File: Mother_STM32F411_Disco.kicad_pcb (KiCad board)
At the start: 2 copper layers, 234 x 132.7 mm, 34 parts, among them U1 ESP32-DEVKIT-V1

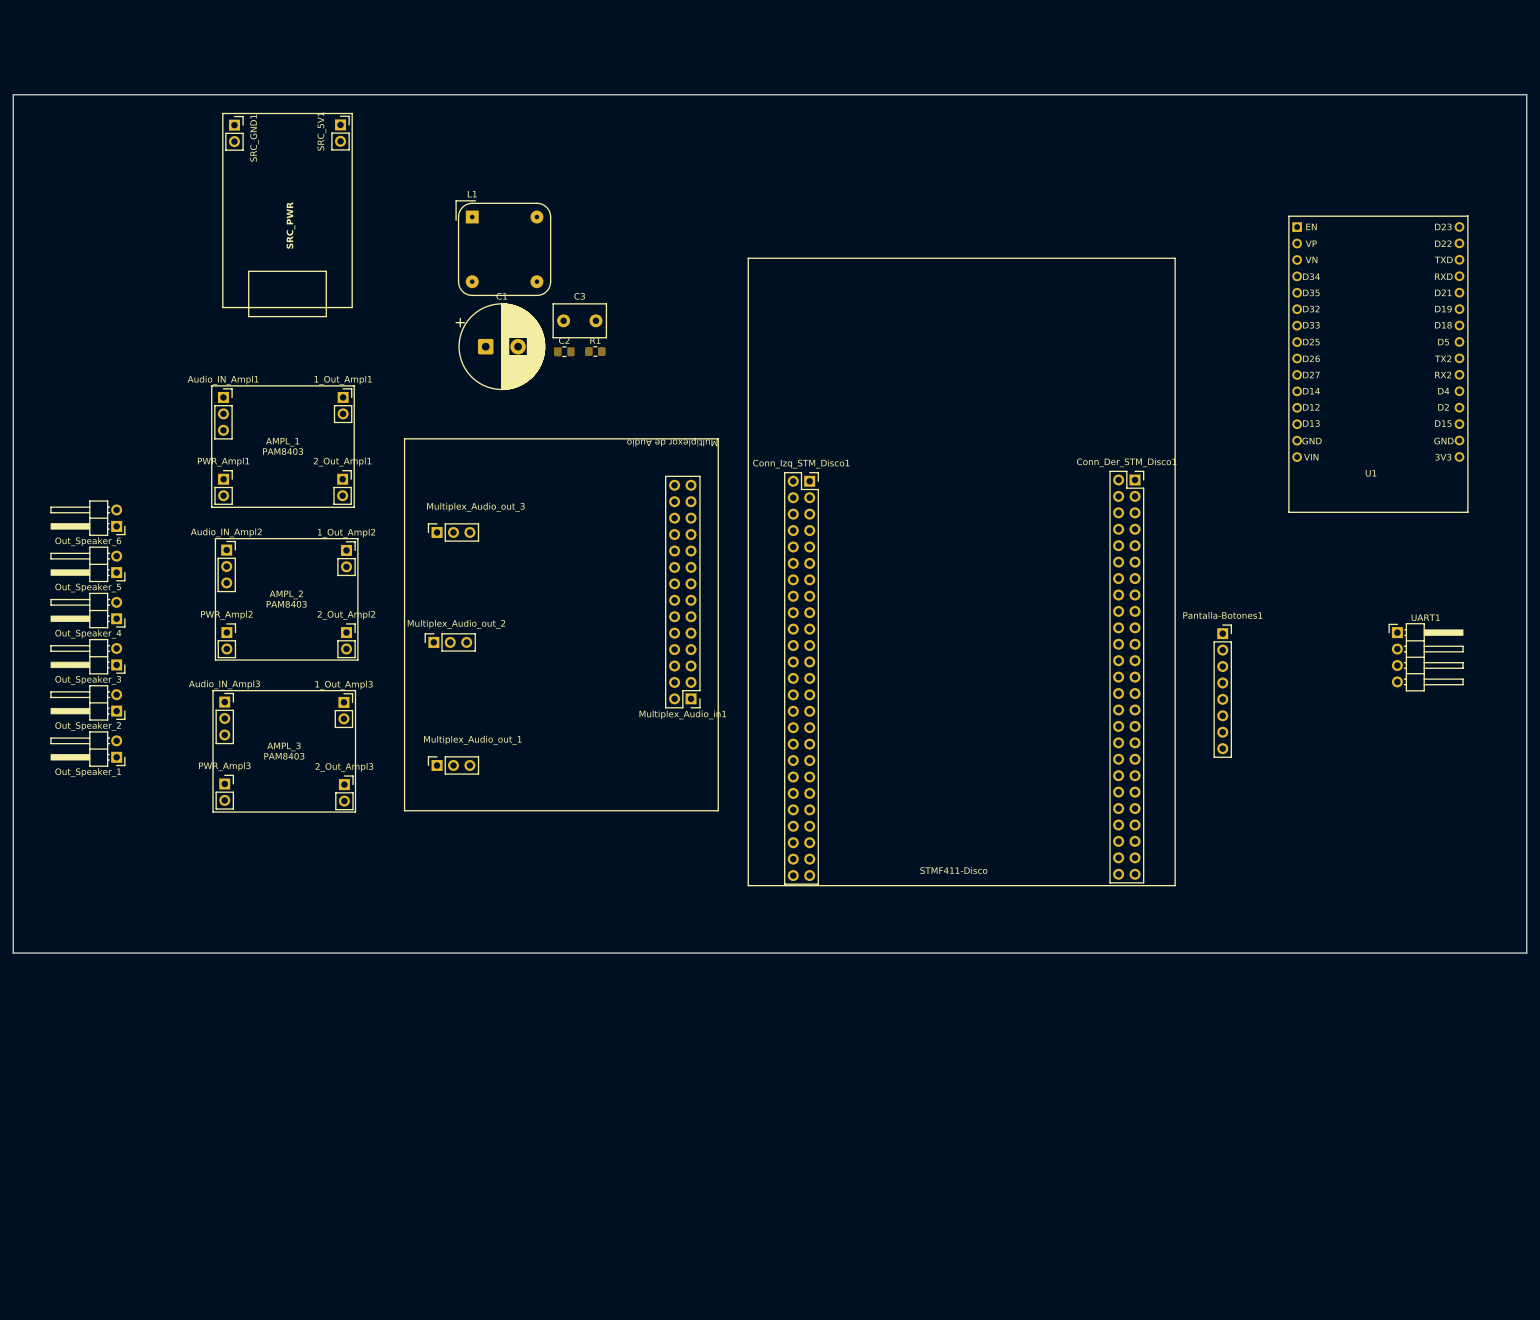
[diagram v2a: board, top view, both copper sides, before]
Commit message: Placa lista para ser routeada con pistas
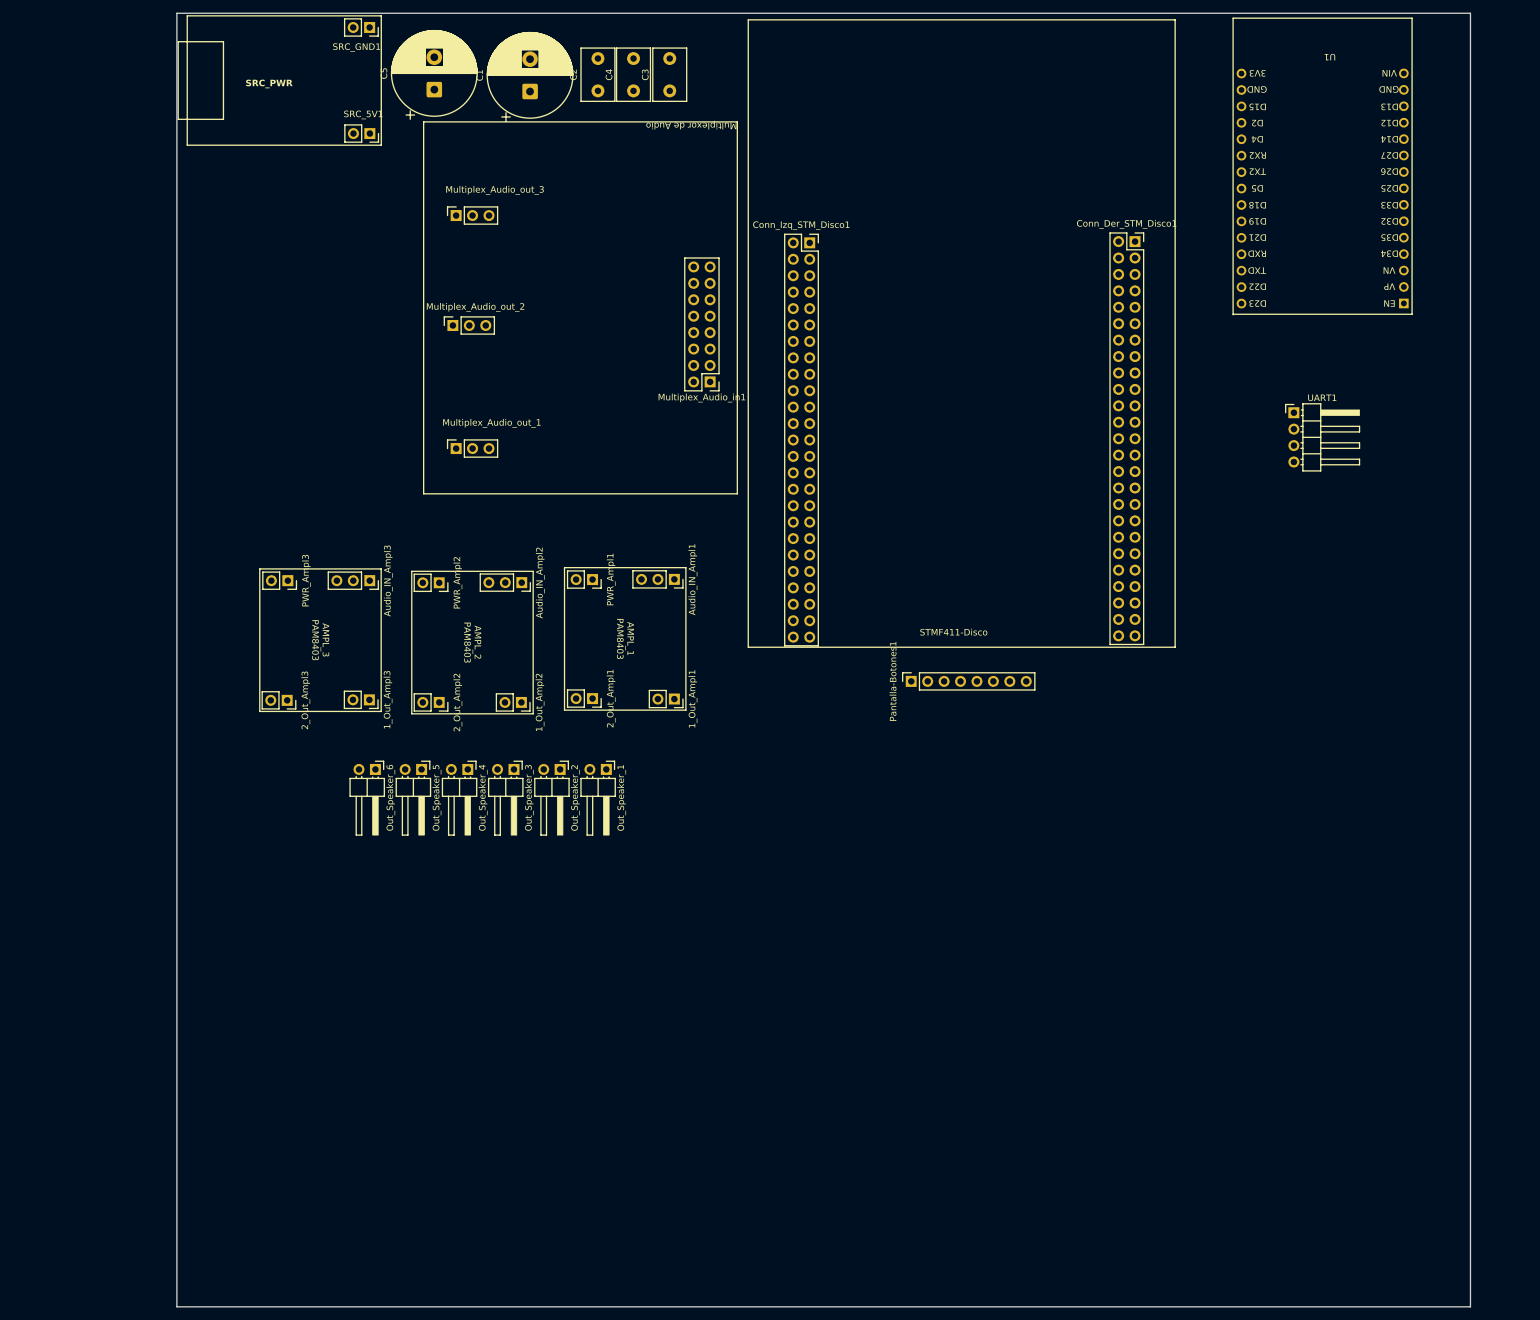
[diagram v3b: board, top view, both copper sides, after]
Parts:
- removed L1: L, Inductor_THT:Choke_Schaffner_RN102-04-14.0x14.0mm
- removed R1: R, Resistor_SMD:R_0805_2012Metric_Pad1.20x1.40mm_HandSolder
- added C4: C, Capacitor_THT:C_Disc_D8.0mm_W5.0mm_P5.00mm, F.Cu at (119.9, 16.7)
- added C5: C, Capacitor_THT:CP_Radial_D13.0mm_P5.00mm, F.Cu at (89.1, 16.5)
- C2: footprint Capacitor_SMD:C_0805_2012Metric_Pad1.18x1.45mm_HandSolder -> Capacitor_THT:C_Disc_D8.0mm_W5.0mm_P5.00mm
- Multiplex_Audio_in1: footprint Connector_PinHeader_2.54mm:PinHeader_2x14_P2.54mm_Vertical -> Connector_PinHeader_2.54mm:PinHeader_2x08_P2.54mm_Vertical
- moved Out_Speaker_1 75.7 mm to (115.7, 121.6), turned to -90 degrees
- moved Audio_IN_Ampl1 75.2 mm to (126.2, 92.2), turned to -90 degrees
- moved 1_Out_Ampl1 69.3 mm to (126.2, 110.7), turned to -90 degrees
- moved Out_Speaker_2 69.2 mm to (108.6, 121.6), turned to -90 degrees
- moved Out_Speaker_3 63.5 mm to (101.4, 121.6), turned to -90 degrees
- moved PWR_Ampl1 59.1 mm to (113.6, 92.3), turned to -90 degrees
- moved Out_Speaker_4 59.1 mm to (94.3, 121.6), turned to -90 degrees
- moved Out_Speaker_5 56.1 mm to (87.1, 121.6), turned to -90 degrees
- moved Out_Speaker_6 54.9 mm to (80.0, 121.6), turned to -90 degrees
- moved 2_Out_Ampl1 51.4 mm to (113.6, 110.7), turned to -90 degrees
- moved Multiplex_Audio_in1 49.1 mm to (131.7, 61.7)
- moved Multiplex_Audio_out_1 49.1 mm to (92.5, 72.0)
- moved Multiplex_Audio_out_2 49.1 mm to (92.0, 53.0)
- moved Multiplex_Audio_out_3 49.1 mm to (92.5, 36.0)
- moved Pantalla-Botones1 48.7 mm to (162.8, 108.0), turned to 90 degrees
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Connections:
- C1 pad 1: Net-(SRC_5V1-Pin_1) -> /5V
- C2 pad 1: /5V_Analog -> /5V
- C3 pad 1: Net-(SRC_5V1-Pin_1) -> /5V
- PWR_Ampl1 pad 2: /VDD -> /5V
- PWR_Ampl2 pad 2: /VDD -> /5V
- PWR_Ampl3 pad 2: /VDD -> /5V
- SRC_5V1 pad 1: Net-(SRC_5V1-Pin_1) -> /5V
- SRC_5V1 pad 2: Net-(SRC_5V1-Pin_1) -> /5V
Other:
- board size 234 x 132.7 mm -> 200 x 200 mm

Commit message: acomodando  pines de la placa stm
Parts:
- Conn_Der_STM_Disco1, Conn_Izq_STM_Disco1: moved to B.Cu
- moved Out_Speaker_1 134.4 mm to (247.0, 150.3)
- moved Out_Speaker_2 128.7 mm to (234.0, 150.3)
- moved Out_Speaker_3 124.9 mm to (223.0, 150.3)
- moved Conn_Der_STM_Disco1 123.1 mm to (318.3, 63.1), turned to 180 degrees
- moved Conn_Izq_STM_Disco1 122.9 mm to (267.9, 63.0), turned to 180 degrees
- moved C5 122.8 mm to (209.8, 39.2)
- moved Pantalla-Botones1 122.8 mm to (283.5, 130.7)
- moved SRC_GND1 122.8 mm to (199.8, 29.6)
- moved 2_Out_Ampl2 122.8 mm to (210.6, 134.0)
- moved 2_Out_Ampl3 122.8 mm to (187.1, 133.6)
- moved Audio_IN_Ampl2 122.8 mm to (223.3, 115.4)
- moved Audio_IN_Ampl3 122.8 mm to (199.8, 115.1)
- moved PWR_Ampl2 122.8 mm to (210.6, 115.5)
- moved PWR_Ampl3 122.8 mm to (187.2, 115.1)
- moved SRC_5V1 122.8 mm to (199.8, 46.0)
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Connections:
- Multiplex_Audio_in1 pad 1: /VDD -> /5V
- Multiplex_Audio_in1 pad 10: /PA4 -> unconnected-(Multiplex_Audio_in1-Pin_10-Pad10)
- Multiplex_Audio_in1 pad 11: /PA2 -> /PA3
- Multiplex_Audio_in1 pad 12: /PA0 -> unconnected-(Multiplex_Audio_in1-Pin_12-Pad12)
- Multiplex_Audio_in1 pad 13: /PC2 -> /PA5
- Multiplex_Audio_in1 pad 14: /PC0 -> unconnected-(Multiplex_Audio_in1-Pin_14-Pad14)
- Multiplex_Audio_in1 pad 15: /NRST -> /PA7
- Multiplex_Audio_in1 pad 16: /VDD -> unconnected-(Multiplex_Audio_in1-Pin_16-Pad16)
- Multiplex_Audio_in1 pad 2: /GND -> unconnected-(Multiplex_Audio_in1-Pin_2-Pad2)
- Multiplex_Audio_in1 pad 3: /PC1 -> /GND
- Multiplex_Audio_in1 pad 4: /PC3 -> unconnected-(Multiplex_Audio_in1-Pin_4-Pad4)
- Multiplex_Audio_in1 pad 5: /PA1 -> /PC1
- Multiplex_Audio_in1 pad 6: /PA3 -> unconnected-(Multiplex_Audio_in1-Pin_6-Pad6)
- Multiplex_Audio_in1 pad 7: /PA5 -> /PC3
- Multiplex_Audio_in1 pad 8: /PA7 -> unconnected-(Multiplex_Audio_in1-Pin_8-Pad8)
- Multiplex_Audio_in1 pad 9: /PA6 -> /PA1
